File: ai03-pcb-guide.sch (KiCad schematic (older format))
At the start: 16 parts

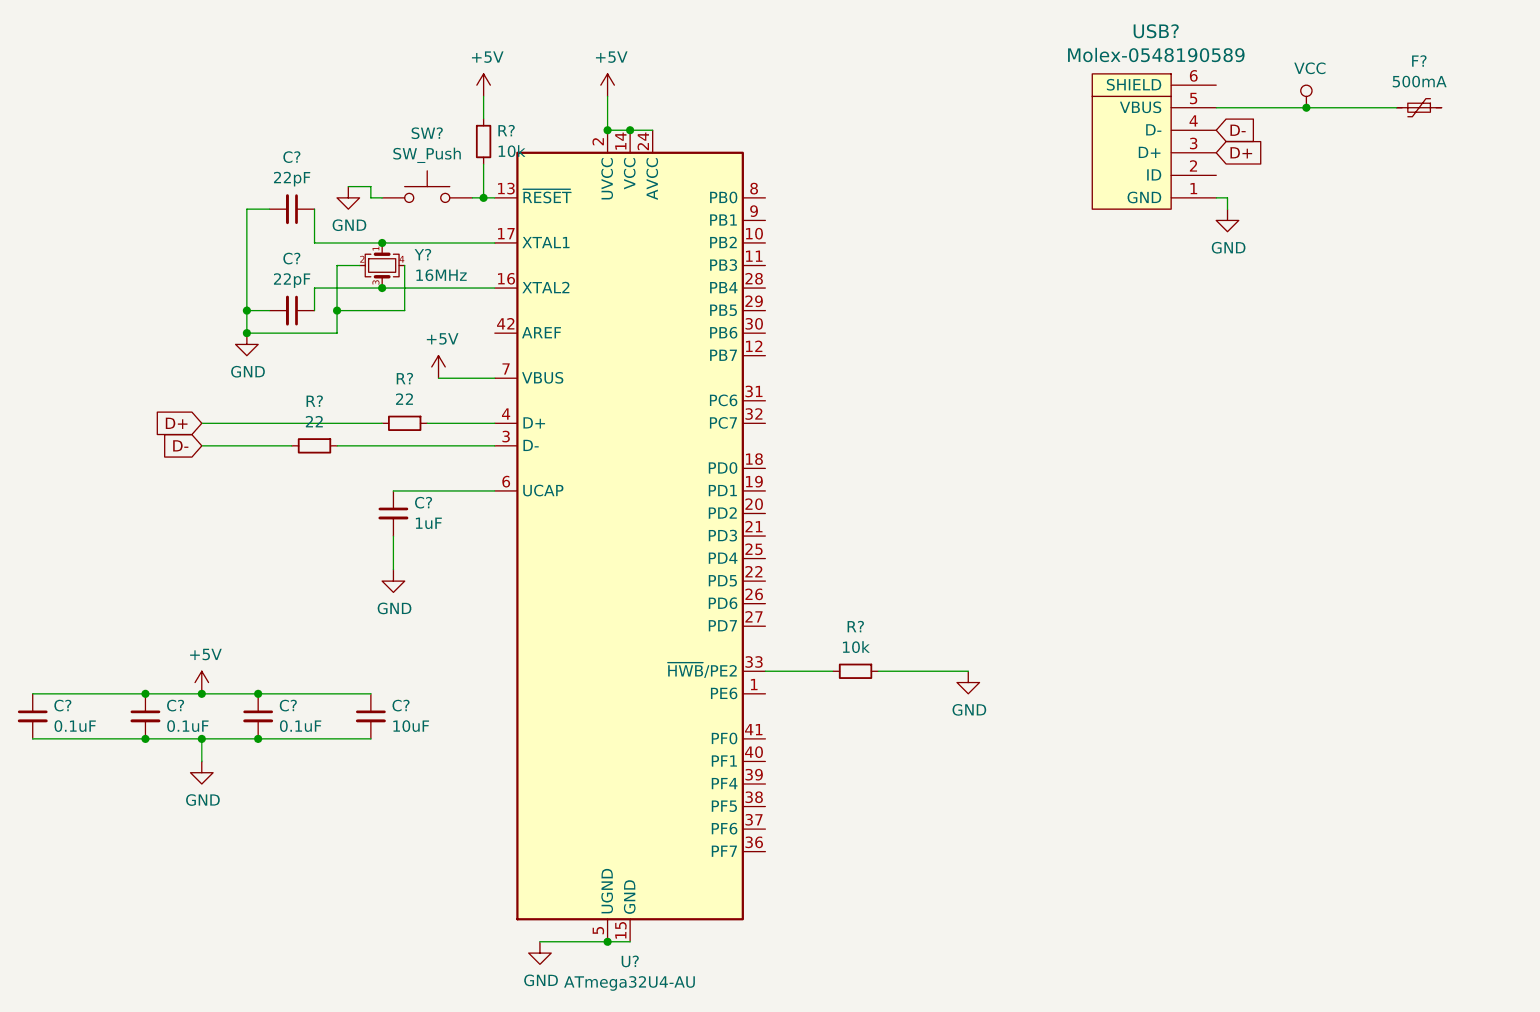
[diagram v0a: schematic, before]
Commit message: Add updated MX submodule
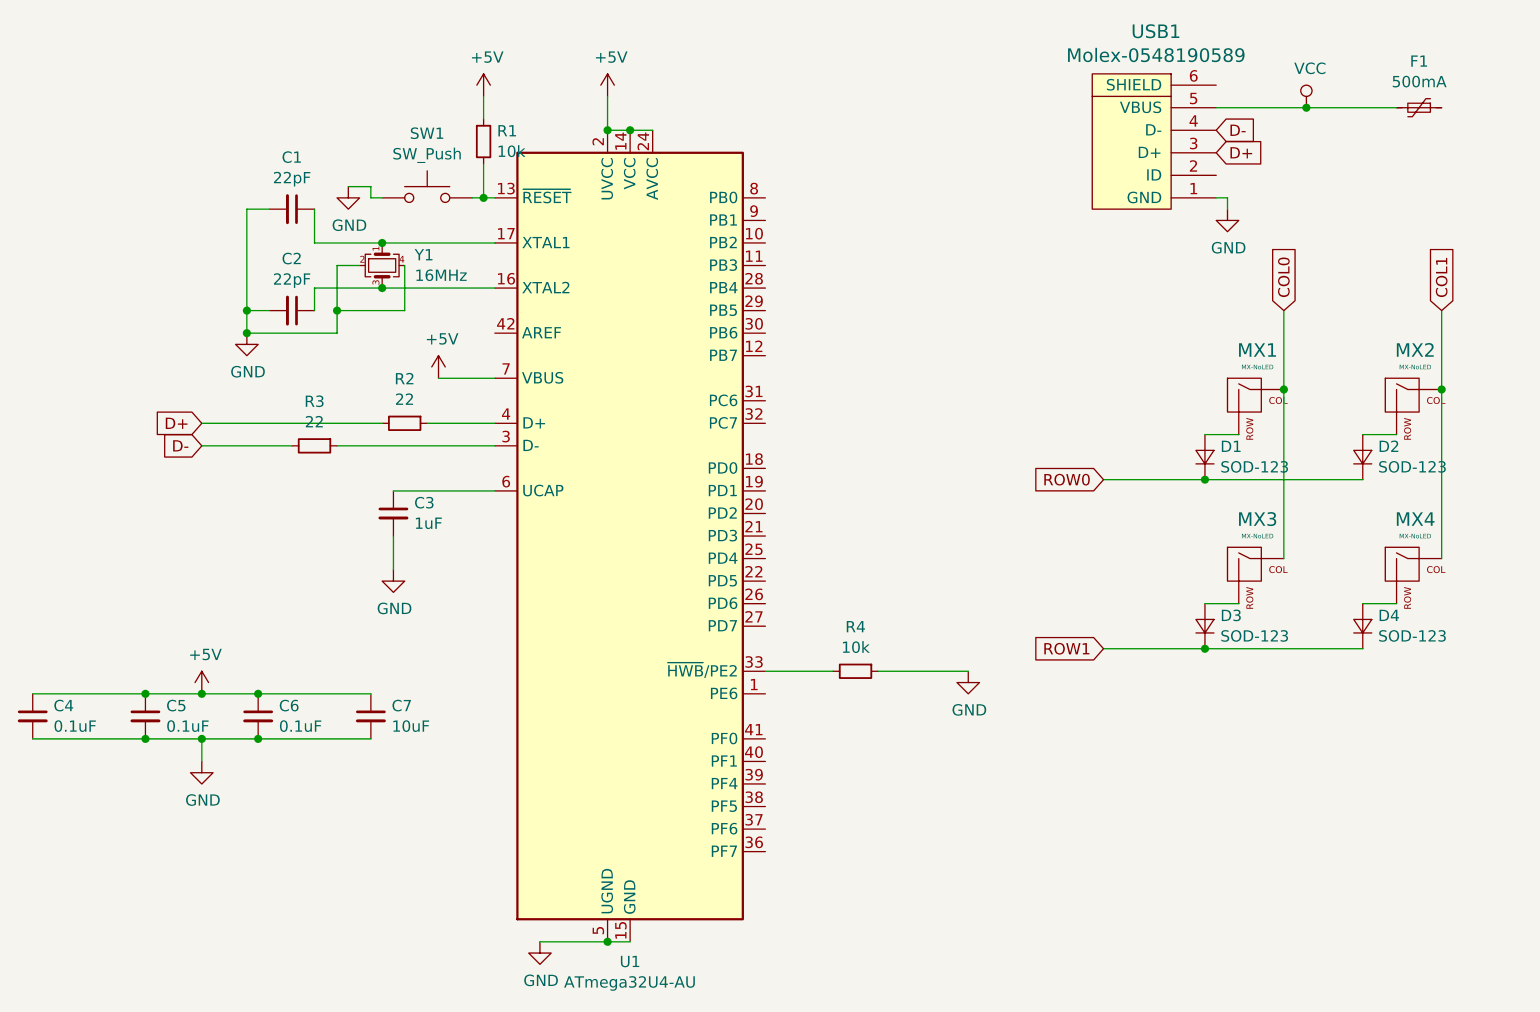
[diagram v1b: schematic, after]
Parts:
- added D1, D2, D3, D4: SOD-123, Diode_SMD:D_SOD-123, symbol Device:D_Small
- added MX1, MX2, MX3, MX4: MX-NoLED, symbol MX_Alps_Hybrid:MX-NoLED
- C1, C2, C3, C4, C5, C6, C7: renamed from C?; footprint (none) -> Capacitor_SMD:C_0805_2012Metric
- F1: renamed from F?; footprint (none) -> Fuse:Fuse_1206_3216Metric
- R1, R2, R3, R4: renamed from R?; footprint (none) -> Resistor_SMD:R_0805_2012Metric
- SW1: renamed from SW?; footprint (none) -> random-keyboard-parts:SKQG-1155865
- USB1: renamed from USB?; footprint (none) -> random-keyboard-parts:Molex-0548190589
- Y1: renamed from Y?; footprint (none) -> Crystal:Crystal_SMD_3225-4Pin_3.2x2.5mm
- gave numbers to parts that had none: 1
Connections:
- new net: D1.2 (A), MX1.2 (ROW)
- new net: D2.2 (A), MX2.2 (ROW)
- new net: D3.2 (A), MX3.2 (ROW)
- new net: D4.2 (A), MX4.2 (ROW)
- new net COL0: MX1.1 (COL), MX3.1 (COL)
- new net COL1: MX2.1 (COL), MX4.1 (COL)
- new net ROW0: D1.1 (K), D2.1 (K)
- new net ROW1: D3.1 (K), D4.1 (K)

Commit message: Completed schematic
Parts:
- MX1, MX2, MX3, MX4: footprint (none) -> MX_Alps_Hybrid:MXOnly-1U
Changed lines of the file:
@@
 	7050 1950 7050 2000
-$Comp
-L MX_Alps_Hybrid:MX-NoLED MX1
-U 1 1 669C3B57
-P 7150 2850
-F 0 "MX1" H 7183 3073 60  0000 C CNN
-F 1 "MX-NoLED" H 7183 2999 20  0000 C CNN
-F 2 "" H 6525 2825 60  0001 C CNN
-F 3 "" H 6525 2825 60  0001 C CNN
-	1    7150 2850
-	1    0    0    -1
-$EndComp
 $Comp
 L Device:D_Small D1
@@
 	7100 3000 6950 3000
 $Comp
-L MX_Alps_Hybrid:MX-NoLED MX2
-U 1 1 669CA95A
-P 7850 2850
-F 0 "MX2" H 7883 3073 60  0000 C CNN
-F 1 "MX-NoLED" H 7883 2999 20  0000 C CNN
-F 2 "" H 7225 2825 60  0001 C CNN
-F 3 "" H 7225 2825 60  0001 C CNN
-	1    7850 2850
-	1    0    0    -1
-$EndComp
-$Comp
 L Device:D_Small D2
 U 1 1 669CA960
@@
 Wire Wire Line
 	7800 3000 7650 3000
-$Comp
-L MX_Alps_Hybrid:MX-NoLED MX3
-U 1 1 669CC961
-P 7150 3600
-F 0 "MX3" H 7183 3823 60  0000 C CNN
-F 1 "MX-NoLED" H 7183 3749 20  0000 C CNN
-F 2 "" H 6525 3575 60  0001 C CNN
-F 3 "" H 6525 3575 60  0001 C CNN
-	1    7150 3600
-	1    0    0    -1
-$EndComp
 $Comp
 L Device:D_Small D3
@@
 	7100 3750 6950 3750
 $Comp
-L MX_Alps_Hybrid:MX-NoLED MX4
-U 1 1 669CDFD0
-P 7850 3600
-F 0 "MX4" H 7883 3823 60  0000 C CNN
-F 1 "MX-NoLED" H 7883 3749 20  0000 C CNN
-F 2 "" H 7225 3575 60  0001 C CNN
-F 3 "" H 7225 3575 60  0001 C CNN
-	1    7850 3600
-	1    0    0    -1
-$EndComp
-$Comp
 L Device:D_Small D4
 U 1 1 669CDFD6
@@
 Wire Wire Line
 	7800 3750 7650 3750
-Wire Wire Line
-	7300 2450 7300 2800
-Connection ~ 7300 2800
-Wire Wire Line
-	7300 2800 7300 3550
-Wire Wire Line
-	8000 2450 8000 2800
-Connection ~ 8000 2800
-Wire Wire Line
-	8000 2800 8000 3550
 Wire Wire Line
 	6500 3200 6950 3200
@@
 Text GLabel 6500 3200 0    50   Input ~ 0
 ROW0
+$Comp
+L MX_Alps_Hybrid:MX-NoLED MX3
+U 1 1 669CC961
+P 7150 3600
+F 0 "MX3" H 7183 3823 60  0000 C CNN
+F 1 "MX-NoLED" H 7183 3749 20  0000 C CNN
+F 2 "MX_Alps_Hybrid:MXOnly-1U" H 6525 3575 60  0001 C CNN
+F 3 "" H 6525 3575 60  0001 C CNN
+	1    7150 3600
+	1    0    0    -1
+$EndComp
+$Comp
+L MX_Alps_Hybrid:MX-NoLED MX4
+U 1 1 669CDFD0
+P 7850 3600
+F 0 "MX4" H 7883 3823 60  0000 C CNN
+F 1 "MX-NoLED" H 7883 3749 20  0000 C CNN
+F 2 "MX_Alps_Hybrid:MXOnly-1U" H 7225 3575 60  0001 C CNN
+F 3 "" H 7225 3575 60  0001 C CNN
+	1    7850 3600
+	1    0    0    -1
+$EndComp
+Wire Wire Line
+	8000 2800 8000 3550
+Wire Wire Line
+	8000 2450 8000 2800
+Connection ~ 8000 2800
+$Comp
+L MX_Alps_Hybrid:MX-NoLED MX2
+U 1 1 669CA95A
+P 7850 2850
+F 0 "MX2" H 7883 3073 60  0000 C CNN
+F 1 "MX-NoLED" H 7883 2999 20  0000 C CNN
+F 2 "MX_Alps_Hybrid:MXOnly-1U" H 7225 2825 60  0001 C CNN
+F 3 "" H 7225 2825 60  0001 C CNN
+	1    7850 2850
+	1    0    0    -1
+$EndComp
 Text GLabel 6500 3950 0    50   Input ~ 0
 ROW1
+Wire Wire Line
+	7300 2800 7300 3550
+Wire Wire Line
+	7300 2450 7300 2800
+Connection ~ 7300 2800
+$Comp
+L MX_Alps_Hybrid:MX-NoLED MX1
+U 1 1 669C3B57
+P 7150 2850
+F 0 "MX1" H 7183 3073 60  0000 C CNN
+F 1 "MX-NoLED" H 7183 2999 20  0000 C CNN
+F 2 "MX_Alps_Hybrid:MXOnly-1U" H 6525 2825 60  0001 C CNN
+F 3 "" H 6525 2825 60  0001 C CNN
+	1    7150 2850
+	1    0    0    -1
+$EndComp
 $EndSCHEMATC

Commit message: PCB Progress
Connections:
- net +5V: now also F1.1
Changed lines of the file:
@@
 	1    0    0    -1
 $EndComp
+$Comp
+L power:+5V #PWR?
+U 1 1 669FE95A
+P 8250 1550
+F 0 "#PWR?" H 8250 1400 50  0001 C CNN
+F 1 "+5V" H 8265 1723 50  0000 C CNN
+F 2 "" H 8250 1550 50  0001 C CNN
+F 3 "" H 8250 1550 50  0001 C CNN
+	1    8250 1550
+	1    0    0    -1
+$EndComp
+Wire Wire Line
+	8000 1550 8250 1550
 $EndSCHEMATC

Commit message: Finalized PCB Design
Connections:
- net COL0: now also U1.29 (PB5)
- net COL1: now also U1.28 (PB4)
- net GND: now also USB1.6 (SHIELD)
- net ROW0: now also U1.27 (PD7)
- net ROW1: now also U1.30 (PB6)
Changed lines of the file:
@@
 $EndComp
 $Comp
-L power:+5V #PWR?
+L power:+5V #PWR0113
 U 1 1 669FE95A
 P 8250 1550
-F 0 "#PWR?" H 8250 1400 50  0001 C CNN
+F 0 "#PWR0113" H 8250 1400 50  0001 C CNN
 F 1 "+5V" H 8265 1723 50  0000 C CNN
 F 2 "" H 8250 1550 50  0001 C CNN
@@
 Wire Wire Line
 	8000 1550 8250 1550
+Text GLabel 5000 3850 2    50   Input ~ 0
+ROW0
+Text GLabel 5000 2550 2    50   Input ~ 0
+ROW1
+Text GLabel 5000 2450 2    50   Input ~ 0
+COL0
+Text GLabel 5000 2350 2    50   Input ~ 0
+COL1
+$Comp
+L power:GND #PWR?
+U 1 1 66A0BE9A
+P 7100 1400
+F 0 "#PWR?" H 7100 1150 50  0001 C CNN
+F 1 "GND" H 7105 1227 50  0000 C CNN
+F 2 "" H 7100 1400 50  0001 C CNN
+F 3 "" H 7100 1400 50  0001 C CNN
+	1    7100 1400
+	1    0    0    -1
+$EndComp
+Wire Wire Line
+	7000 1450 7000 1400
+Wire Wire Line
+	7000 1400 7100 1400
 $EndSCHEMATC
